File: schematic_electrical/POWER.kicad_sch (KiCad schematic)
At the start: 5 parts, among them SW1 WGCD_SPST_ILLUM_TOGGLE, SW2 WGCD_SPST_ILLUM_TOGGLE

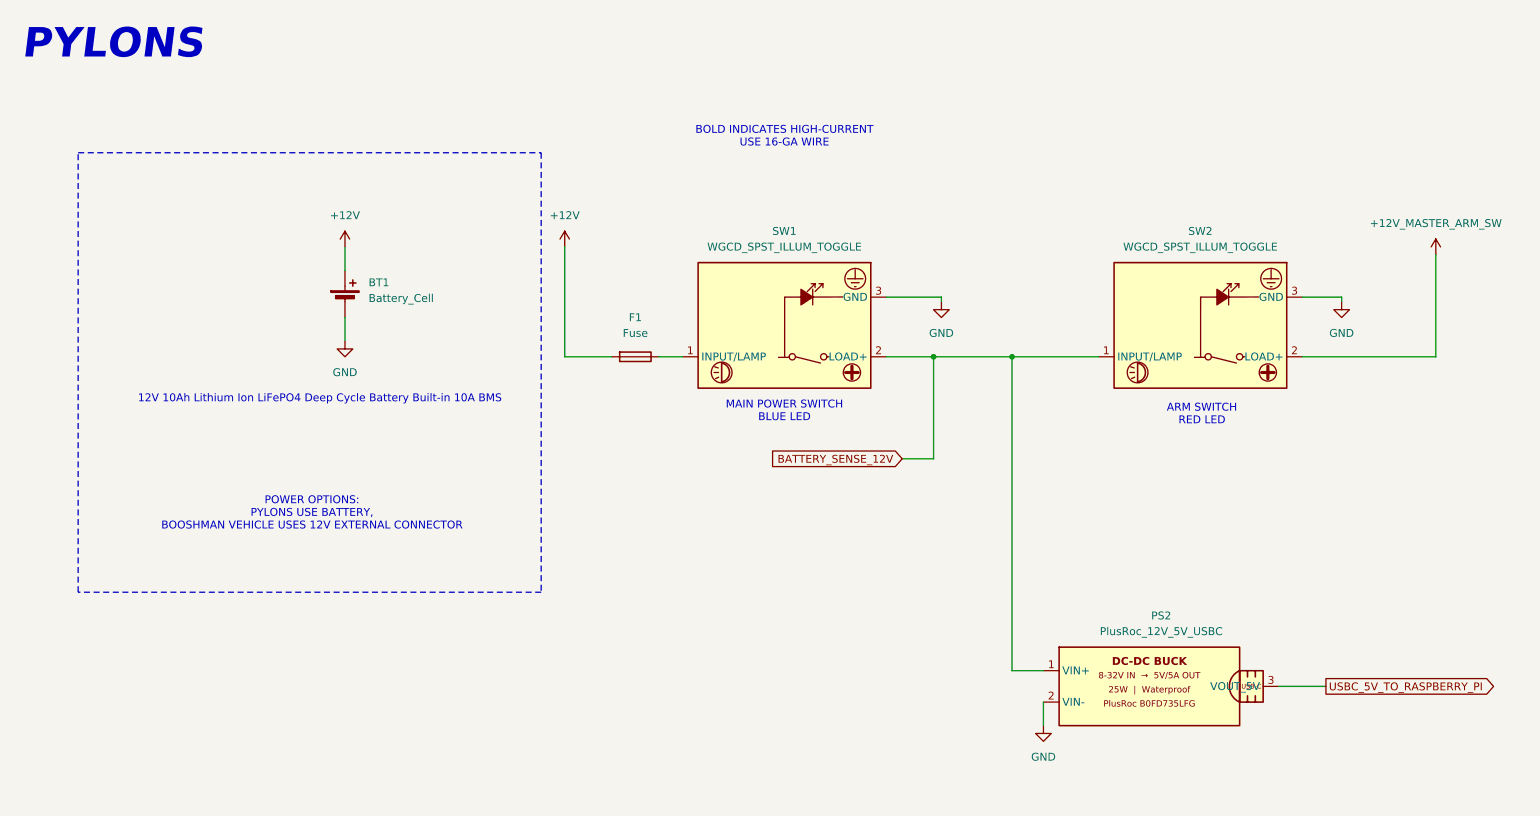
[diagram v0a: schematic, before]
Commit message: Add expansion buttons/lamps schematic sheet; schematic cleanup and annotations
- New EXPANSION_BUTTONS_LAMPS.kicad_sch sheet wired into top-level schematic
- Add AB_800T-QT24 symbol library
- ESP32_MCU: wire previously unconnected GPIO pins to BUTTON0-4 and BUTTON_LAMP_PWM_OUT0-4 global labels; add expansion IO bounding box annotation
- POWER: add GND ganging fabrication notes, DCDC USB wiring note, fuse value updated to "10A MINI AUTO BLADE"; routing cleanup
- CONNECTORS: routing and junction cleanup
- BOOSH_TRIGGER: remove stale "1R" errata note
- IDEA.md: add sandbox notes and open questions

Co-Authored-By: Claude Sonnet 4.6 <noreply@anthropic.com>
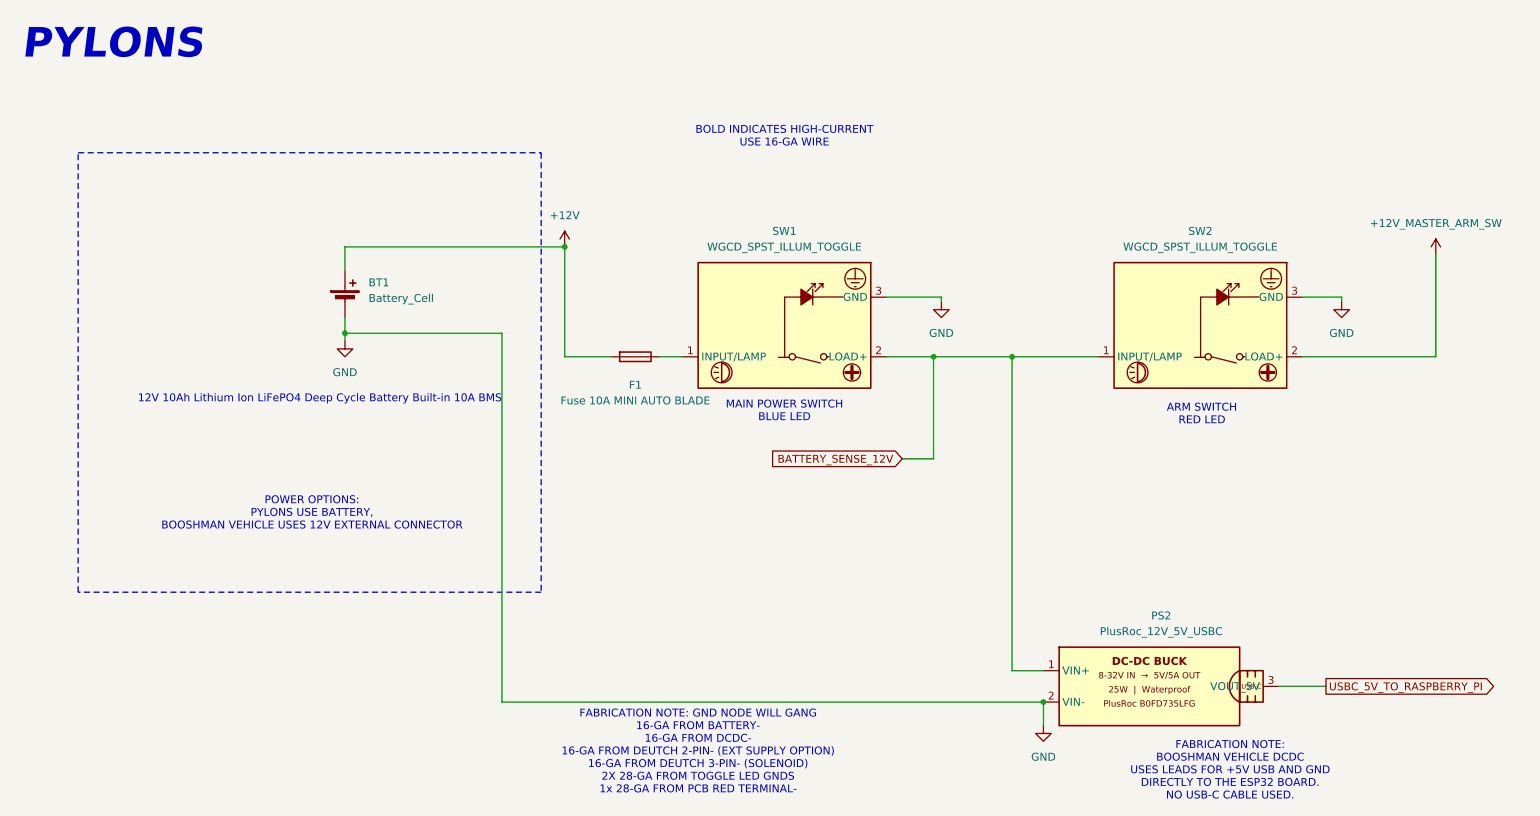
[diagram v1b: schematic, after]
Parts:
- F1: value Fuse -> Fuse 10A MINI AUTO BLADE
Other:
- note added: "FABRICATION NOTE: BOOSHMAN VEHICLE DCDC USES LEADS FOR +5V USB AND GND DIRECTLY TO THE ESP32 BOARD. NO USB-C CABLE USED."
- note added: "FABRICATION NOTE: GND NODE WILL GANG 16-GA FROM BATTERY- 16-GA FROM DCDC- 16-GA FROM DEUTCH 2-PIN- (EXT SUPPLY OPTION) 16-GA FROM DEUTCH 3-PIN- (SOLENOID) 2X 28-GA FROM TOGGLE LED GNDS 1x 28-GA FROM PCB RED TERMINAL-"
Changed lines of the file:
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@@
 	(paper "A4")
+	(junction
+		(at 107.95 54.61)
+		(diameter 0)
+		(color 0 0 0 0)
+	)
+	(junction
+		(at 185.42 128.27)
+		(diameter 0)
+		(color 0 0 0 0)
+	)
 	(junction
 		(at 180.34 72.39)
@@
 	)
 	(junction
+		(at 72.39 68.58)
+		(diameter 0)
+		(color 0 0 0 0)
+	)
+	(junction
 		(at 167.64 72.39)
 		(diameter 0)
@@
 	(wire
 		(pts
+			(xy 185.42 128.27) (xy 97.79 128.27)
+		)
+		(stroke
+			(width 0.508)
+			(type default)
+		)
+	)
+	(wire
+		(pts
+			(xy 97.79 128.27) (xy 97.79 68.58)
+		)
+		(stroke
+			(width 0.508)
+			(type default)
+		)
+	)
+	(wire
+		(pts
 			(xy 180.34 123.19) (xy 185.42 123.19)
 		)
@@
 	(wire
 		(pts
+			(xy 97.79 68.58) (xy 72.39 68.58)
+		)
+		(stroke
+			(width 0.508)
+			(type default)
+		)
+	)
+	(wire
+		(pts
 			(xy 248.92 72.39) (xy 248.92 55.88)
 		)
@@
 	(wire
 		(pts
-			(xy 72.39 66.04) (xy 72.39 69.85)
+			(xy 72.39 66.04) (xy 72.39 68.58)
 		)
 		(stroke
@@
 	(wire
 		(pts
+			(xy 72.39 54.61) (xy 107.95 54.61)
+		)
+		(stroke
+			(width 0.508)
+			(type default)
+		)
+	)
+	(wire
+		(pts
 			(xy 162.56 88.9) (xy 167.64 88.9)
 		)
@@
 		(pts
 			(xy 227.33 72.39) (xy 248.92 72.39)
+		)
+		(stroke
+			(width 0.508)
+			(type default)
+		)
+	)
+	(wire
+		(pts
+			(xy 72.39 68.58) (xy 72.39 69.85)
 		)
 		(stroke
@@
 		)
 	)
+	(text "FABRICATION NOTE: GND NODE WILL GANG\n16-GA FROM BATTERY-\n16-GA FROM DCDC-\n16-GA FROM DEUTCH 2-PIN- (EXT SUPPLY OPTION)\n16-GA FROM DEUTCH 3-PIN- (SOLENOID)\n2X 28-GA FROM TOGGLE LED GNDS\n1x 28-GA FROM PCB RED TERMINAL-"
+		(exclude_from_sim no)
+		(at 129.54 136.398 0)
+		(effects
+			(font
+				(size 1.27 1.27)
+			)
+		)
+	)
 	(text "ARM SWITCH\nRED LED"
 		(exclude_from_sim no)
@@
 		(exclude_from_sim no)
 		(at 143.51 36.83 0)
+		(effects
+			(font
+				(size 1.27 1.27)
+			)
+		)
+	)
+	(text "FABRICATION NOTE: \nBOOSHMAN VEHICLE DCDC\nUSES LEADS FOR +5V USB AND GND\nDIRECTLY TO THE ESP32 BOARD.\nNO USB-C CABLE USED."
+		(exclude_from_sim no)
+		(at 215.646 139.446 0)
 		(effects
 			(font
@@
 				(justify right)
 				(hide yes)
-			)
-		)
-	)
-	(symbol
-		(lib_id "power:+12V")
-		(at 72.39 54.61 0)
-		(unit 1)
-		(exclude_from_sim no)
-		(in_bom yes)
-		(on_board yes)
-		(dnp no)
-		(fields_autoplaced yes)
-		(property "Reference" "#PWR03"
-			(at 72.39 58.42 0)
-			(effects
-				(font
-					(size 1.27 1.27)
-				)
-				(hide yes)
-			)
-		)
-		(property "Value" "+12V"
-			(at 72.39 49.53 0)
-			(effects
-				(font
-					(size 1.27 1.27)
-				)
-			)
-		)
-		(property "Footprint" ""
-			(at 72.39 54.61 0)
-			(effects
-				(font
-					(size 1.27 1.27)
-				)
-				(hide yes)
-			)
-		)
-		(property "Datasheet" ""
-			(at 72.39 54.61 0)
-			(effects
-				(font
-					(size 1.27 1.27)
-				)
-				(hide yes)
-			)
-		)
-		(property "Description" "Power symbol creates a global label with name \"+12V\""
-			(at 72.39 54.61 0)
-			(effects
-				(font
-					(size 1.27 1.27)
-				)
-				(hide yes)
-			)
-		)
-		(pin "1"
-		)
-		(instances
-			(project "pylons_boosh_remote_reciver"
-				(path "/f3653ac0-a28a-4ee8-bcf5-236139001455/6657731a-46b5-42dc-8611-bac46a2b6e5c"
-					(reference "#PWR03")
-					(unit 1)
-				)
 			)
 		)
@@
 		(on_board yes)
 		(dnp no)
-		(fields_autoplaced yes)
 		(property "Reference" "F1"
-			(at 119.38 66.04 90)
-			(effects
-				(font
-					(size 1.27 1.27)
-				)
-			)
-		)
-		(property "Value" "Fuse"
-			(at 119.38 68.58 90)
-			(effects
-				(font
+			(at 119.38 76.962 90)
+			(effects
+				(font
+					(size 1.27 1.27)
+				)
+			)
+		)
+		(property "Value" "Fuse 10A MINI AUTO BLADE"
+			(at 119.38 79.502 90)
+			(effects
+				(font
